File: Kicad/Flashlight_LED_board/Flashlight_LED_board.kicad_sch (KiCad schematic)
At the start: 10 parts, among them IC1 ISL78100ARZ

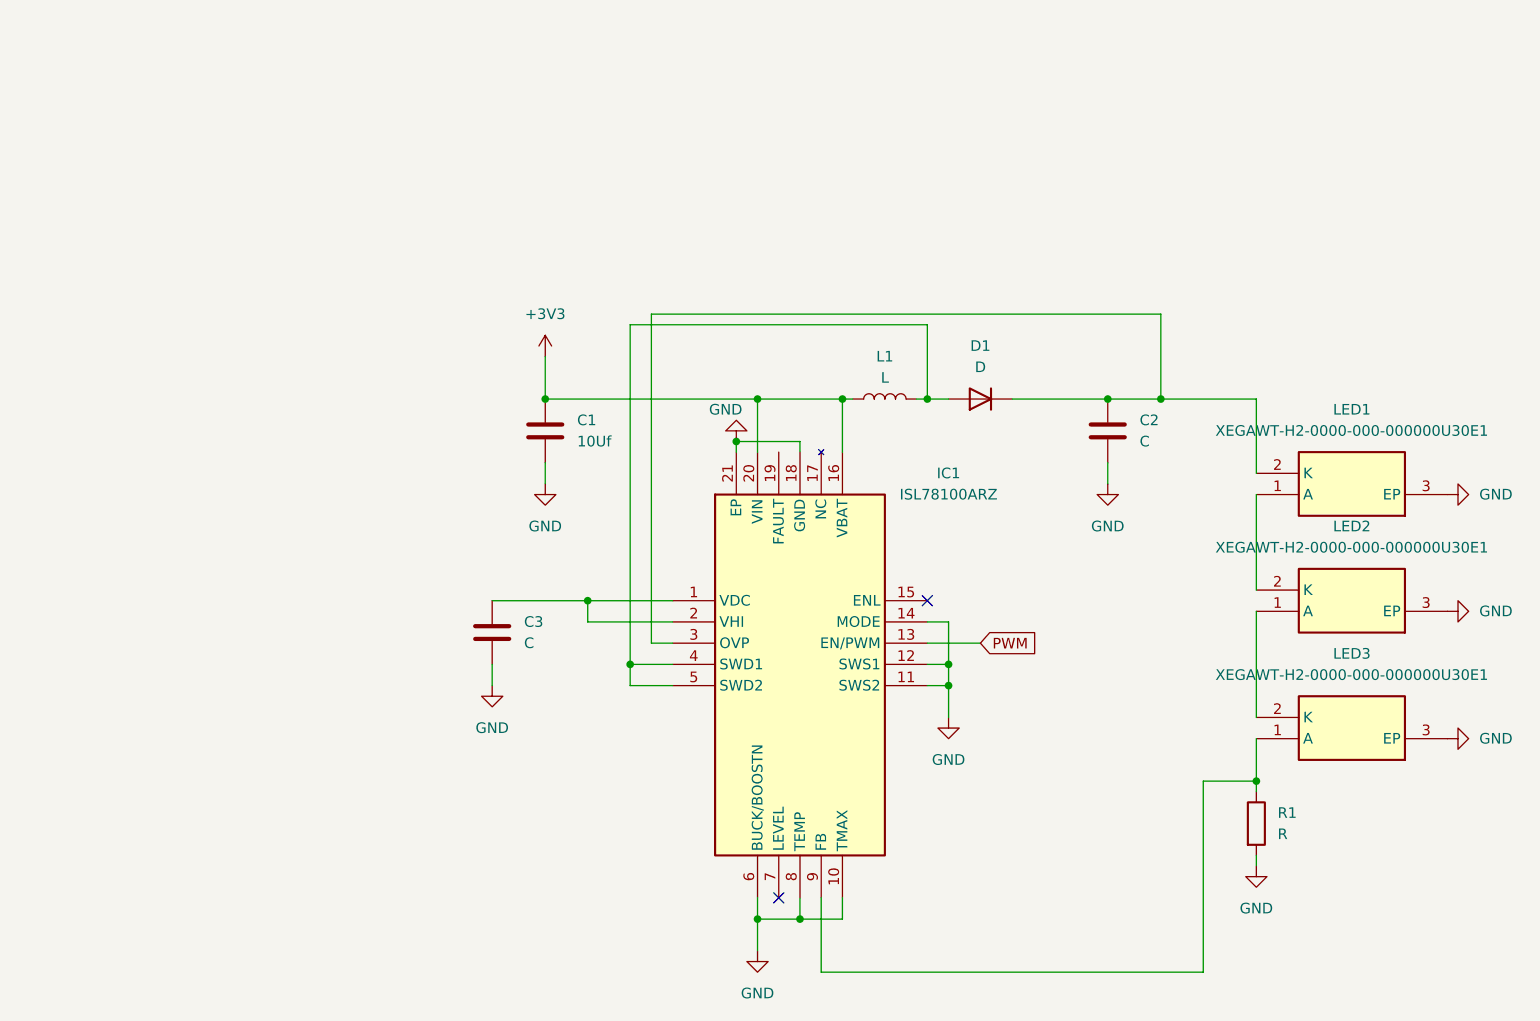
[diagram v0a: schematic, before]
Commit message: cosmetic work on tof
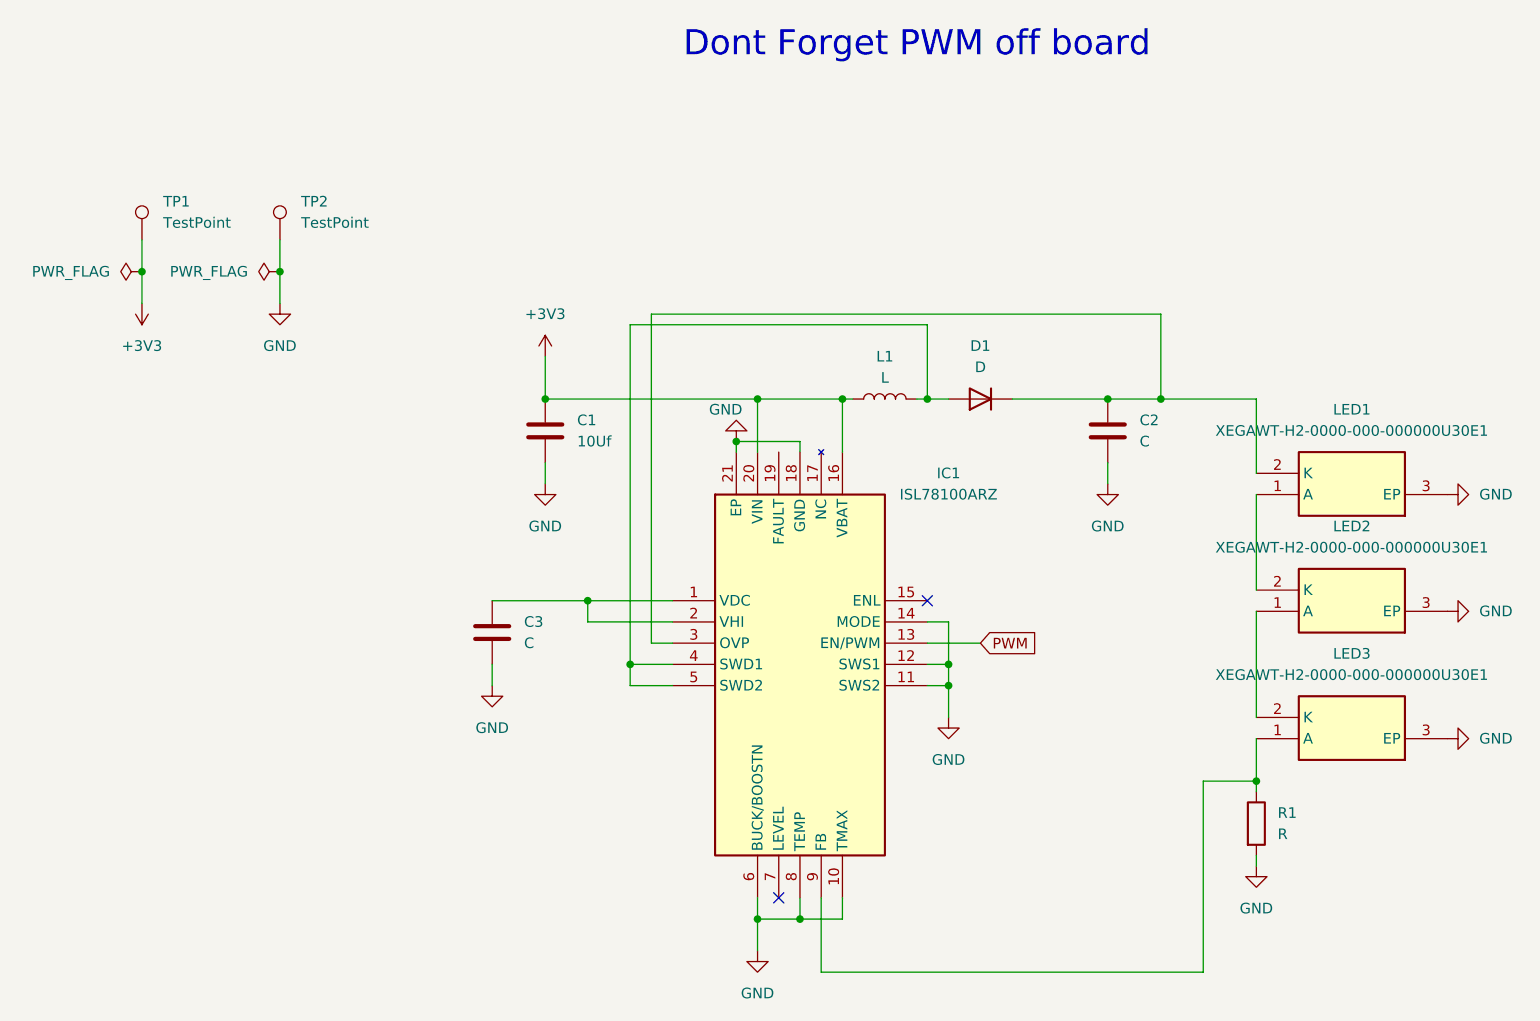
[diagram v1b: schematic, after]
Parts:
- added TP1, TP2: TestPoint, TestPoint:TestPoint_Pad_2.5x2.5mm, symbol Connector:TestPoint
- IC1: footprint QFN50P400X400X100-21N -> SamacSys_Parts:PI4ULS3V204ZBEX
- LED1, LED2, LED3: footprint XEGAWTH20000000000000U30E1 -> SamacSys_Parts:XEGAWTH20000000000000U30E1
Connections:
- net +3V3: now also TP1.1
- net GND: now also TP2.1
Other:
- note added: "Dont Forget PWM off board"
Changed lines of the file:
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@@
   (junction (at 106.68 81.28) (diameter 0) (color 0 0 0 0)
   )
+  (junction (at 52.07 60.96) (diameter 0) (color 0 0 0 0)
+  )
   (junction (at 109.22 76.2) (diameter 0) (color 0 0 0 0)
   )
@@
   )
   (junction (at 168.91 121.92) (diameter 0) (color 0 0 0 0)
+  )
+  (junction (at 35.56 60.96) (diameter 0) (color 0 0 0 0)
   )
   (junction (at 132.08 107.95) (diameter 0) (color 0 0 0 0)
@@
     (stroke (width 0) (type default))
   )
+  (wire (pts (xy 35.56 64.77) (xy 35.56 60.96))
+    (stroke (width 0) (type default))
+  )
   (wire (pts (xy 128.27 76.2) (xy 129.54 76.2))
     (stroke (width 0) (type default))
   )
+  (wire (pts (xy 52.07 60.96) (xy 52.07 57.15))
+    (stroke (width 0) (type default))
+  )
   (wire (pts (xy 168.91 132.08) (xy 168.91 130.81))
     (stroke (width 0) (type default))
@@
     (stroke (width 0) (type default))
   )
+  (wire (pts (xy 35.56 60.96) (xy 35.56 57.15))
+    (stroke (width 0) (type default))
+  )
+  (wire (pts (xy 52.07 64.77) (xy 52.07 60.96))
+    (stroke (width 0) (type default))
+  )
   (wire (pts (xy 77.47 110.49) (xy 77.47 107.95))
     (stroke (width 0) (type default))
@@
   (wire (pts (xy 129.54 67.31) (xy 129.54 76.2))
     (stroke (width 0) (type default))
+  )
+  (text "Dont Forget PWM off board\n" (at 100.33 35.56 0)
+    (effects (font (size 3 3)) (justify left bottom))
   )
   (global_label "PWM" (shape input) (at 135.89 105.41 0) (fields_autoplaced)
@@
     )
   )
+  (symbol (lib_id "power:PWR_FLAG") (at 52.07 60.96 90) (unit 1)
+    (in_bom yes) (on_board yes) (dnp no) (fields_autoplaced)
+    (property "Reference" "#FLG02" (at 50.165 60.96 0)
+      (effects (font (size 1.27 1.27)) hide)
+    )
+    (property "Value" "PWR_FLAG" (at 48.26 60.96 90)
+      (effects (font (size 1.27 1.27)) (justify left))
+    )
+    (property "Footprint" "" (at 52.07 60.96 0)
+      (effects (font (size 1.27 1.27)) hide)
+    )
+    (property "Datasheet" "~" (at 52.07 60.96 0)
+      (effects (font (size 1.27 1.27)) hide)
+    )
+    (pin "1")
+    (instances
+      (project "Flashlight_LED_board"
+        (path "/6257d396-21b7-43a8-96cc-8bc327006e0c"
+          (reference "#FLG02") (unit 1)
+        )
+      )
+    )
+  )
   (symbol (lib_id "power:GND") (at 132.08 114.3 0) (unit 1)
     (in_bom yes) (on_board yes) (dnp no) (fields_autoplaced)
@@
       (effects (font (size 1.27 1.27)))
     )
-    (property "Footprint" "XEGAWTH20000000000000U30E1" (at 172.72 -7.29 0)
+    (property "Footprint" "SamacSys_Parts:XEGAWTH20000000000000U30E1" (at 172.72 -7.29 0)
       (effects (font (size 1.27 1.27)) (justify left top) hide)
     )
@@
     )
   )
+  (symbol (lib_id "power:PWR_FLAG") (at 35.56 60.96 90) (unit 1)
+    (in_bom yes) (on_board yes) (dnp no) (fields_autoplaced)
+    (property "Reference" "#FLG01" (at 33.655 60.96 0)
+      (effects (font (size 1.27 1.27)) hide)
+    )
+    (property "Value" "PWR_FLAG" (at 31.75 60.96 90)
+      (effects (font (size 1.27 1.27)) (justify left))
+    )
+    (property "Footprint" "" (at 35.56 60.96 0)
+      (effects (font (size 1.27 1.27)) hide)
+    )
+    (property "Datasheet" "~" (at 35.56 60.96 0)
+      (effects (font (size 1.27 1.27)) hide)
+    )
+    (pin "1")
+    (instances
+      (project "Flashlight_LED_board"
+        (path "/6257d396-21b7-43a8-96cc-8bc327006e0c"
+          (reference "#FLG01") (unit 1)
+        )
+      )
+    )
+  )
   (symbol (lib_id "Device:C") (at 77.47 104.14 0) (unit 1)
     (in_bom yes) (on_board yes) (dnp no) (fields_autoplaced)
@@
         (path "/6257d396-21b7-43a8-96cc-8bc327006e0c"
           (reference "#PWR02") (unit 1)
+        )
+      )
+    )
+  )
+  (symbol (lib_id "power:GND") (at 52.07 64.77 0) (unit 1)
+    (in_bom yes) (on_board yes) (dnp no) (fields_autoplaced)
+    (property "Reference" "#PWR013" (at 52.07 71.12 0)
+      (effects (font (size 1.27 1.27)) hide)
+    )
+    (property "Value" "GND" (at 52.07 69.85 0)
+      (effects (font (size 1.27 1.27)))
+    )
+    (property "Footprint" "" (at 52.07 64.77 0)
+      (effects (font (size 1.27 1.27)) hide)
+    )
+    (property "Datasheet" "" (at 52.07 64.77 0)
+      (effects (font (size 1.27 1.27)) hide)
+    )
+    (pin "1")
+    (instances
+      (project "Flashlight_LED_board"
+        (path "/6257d396-21b7-43a8-96cc-8bc327006e0c"
+          (reference "#PWR013") (unit 1)
         )
       )
@@
       (effects (font (size 1.27 1.27)))
     )
-    (property "Footprint" "QFN50P400X400X100-21N" (at 125.73 185.09 0)
+    (property "Footprint" "SamacSys_Parts:PI4ULS3V204ZBEX" (at 125.73 185.09 0)
       (effects (font (size 1.27 1.27)) (justify left top) hide)
     )
@@
     )
   )
+  (symbol (lib_id "Connector:TestPoint") (at 35.56 57.15 0) (unit 1)
+    (in_bom yes) (on_board yes) (dnp no) (fields_autoplaced)
+    (property "Reference" "TP1" (at 38.1 52.578 0)
+      (effects (font (size 1.27 1.27)) (justify left))
+    )
+    (property "Value" "TestPoint" (at 38.1 55.118 0)
+      (effects (font (size 1.27 1.27)) (justify left))
+    )
+    (property "Footprint" "TestPoint:TestPoint_Pad_2.5x2.5mm" (at 40.64 57.15 0)
+      (effects (font (size 1.27 1.27)) hide)
+    )
+    (property "Datasheet" "~" (at 40.64 57.15 0)
+      (effects (font (size 1.27 1.27)) hide)
+    )
+    (pin "1")
+    (instances
+      (project "Flashlight_LED_board"
+        (path "/6257d396-21b7-43a8-96cc-8bc327006e0c"
+          (reference "TP1") (unit 1)
+        )
+      )
+    )
+  )
   (symbol (lib_id "power:GND") (at 191.77 101.6 90) (unit 1)
     (in_bom yes) (on_board yes) (dnp no) (fields_autoplaced)
@@
     )
   )
+  (symbol (lib_id "power:+3V3") (at 35.56 64.77 180) (unit 1)
+    (in_bom yes) (on_board yes) (dnp no) (fields_autoplaced)
+    (property "Reference" "#PWR011" (at 35.56 60.96 0)
+      (effects (font (size 1.27 1.27)) hide)
+    )
+    (property "Value" "+3V3" (at 35.56 69.85 0)
+      (effects (font (size 1.27 1.27)))
+    )
+    (property "Footprint" "" (at 35.56 64.77 0)
+      (effects (font (size 1.27 1.27)) hide)
+    )
+    (property "Datasheet" "" (at 35.56 64.77 0)
+      (effects (font (size 1.27 1.27)) hide)
+    )
+    (pin "1")
+    (instances
+      (project "Flashlight_LED_board"
+        (path "/6257d396-21b7-43a8-96cc-8bc327006e0c"
+          (reference "#PWR011") (unit 1)
+        )
+      )
+    )
+  )
   (symbol (lib_id "Device:R") (at 168.91 127 0) (unit 1)
     (in_bom yes) (on_board yes) (dnp no) (fields_autoplaced)
@@
       (effects (font (size 1.27 1.27)))
     )
-    (property "Footprint" "XEGAWTH20000000000000U30E1" (at 172.72 6.68 0)
+    (property "Footprint" "SamacSys_Parts:XEGAWTH20000000000000U30E1" (at 172.72 6.68 0)
       (effects (font (size 1.27 1.27)) (justify left top) hide)
     )
@@
       (effects (font (size 1.27 1.27)))
     )
-    (property "Footprint" "XEGAWTH20000000000000U30E1" (at 172.72 21.92 0)
+    (property "Footprint" "SamacSys_Parts:XEGAWTH20000000000000U30E1" (at 172.72 21.92 0)
       (effects (font (size 1.27 1.27)) (justify left top) hide)
     )
@@
         )
       )
+    )
+  )
+  (symbol (lib_id "Connector:TestPoint") (at 52.07 57.15 0) (unit 1)
+    (in_bom yes) (on_board yes) (dnp no) (fields_autoplaced)
+    (property "Reference" "TP2" (at 54.61 52.578 0)
+      (effects (font (size 1.27 1.27)) (justify left))
+    )
+    (property "Value" "TestPoint" (at 54.61 55.118 0)
+      (effects (font (size 1.27 1.27)) (justify left))
+    )
+    (property "Footprint" "TestPoint:TestPoint_Pad_2.5x2.5mm" (at 57.15 57.15 0)
+      (effects (font (size 1.27 1.27)) hide)
+    )
+    (property "Datasheet" "~" (at 57.15 57.15 0)
+      (effects (font (size 1.27 1.27)) hide)
+    )
+    (pin "1")
+    (instances
+      (project "Flashlight_LED_board"
+        (path "/6257d396-21b7-43a8-96cc-8bc327006e0c"
+          (reference "TP2") (unit 1)
+        )
+      )
